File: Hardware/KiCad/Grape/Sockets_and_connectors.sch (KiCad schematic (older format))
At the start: 0 parts

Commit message: Alimentacion terminada
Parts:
- added P1, P10, P11, P12, P13, P14, P15, P16, P17, P18, P19, P2, P20, P21, P22, P3, P4, P5, P6, P7, P8, P9: CONN_01X03, symbol CONN_01X03
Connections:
- new net +5V: P1.2 (P2), P10.2 (P2), P11.2 (P2), P12.2 (P2), P13.2 (P2), P14.2 (P2), P15.2 (P2), P16.2 (P2), P17.2 (P2), P18.2 (P2), P19.2 (P2), P2.2 (P2), P20.2 (P2), P21.2 (P2), P22.2 (P2), P3.2 (P2), P4.2 (P2), P5.2 (P2), P6.2 (P2), P7.2 (P2), P8.2 (P2), P9.2 (P2)
- new net GND: P1.3 (P3), P10.3 (P3), P11.3 (P3), P12.3 (P3), P13.3 (P3), P14.3 (P3), P15.3 (P3), P16.3 (P3), P17.3 (P3), P18.3 (P3), P19.3 (P3), P2.3 (P3), P20.3 (P3), P21.3 (P3), P22.3 (P3), P3.3 (P3), P4.3 (P3), P5.3 (P3), P6.3 (P3), P7.3 (P3), P8.3 (P3), P9.3 (P3)

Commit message: Esquema terminado y  ERC pasado
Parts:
- added P23: I2C, symbol CONN_01X04
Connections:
- net +5V: now also P23.3 (P3)
- net GND: now also P23.4 (P4)
- net RX: now reaches P1.1 (P1)
- net TX: now reaches P6.1 (P1)
- net IO2/PIN2: now reaches P11.1 (P1)
- net IO3/PIN3: now reaches P15.1 (P1)
- net IO4/PIN4: now reaches P19.1 (P1)
- net IO5/PIN5: now reaches P2.1 (P1)
- net IO6/PIN6: now reaches P7.1 (P1)
- net IO7/PIN7: now reaches P12.1 (P1)
- net IO8/PIN8: now reaches P16.1 (P1)
- net IO9/PIN9: now reaches P20.1 (P1)
- net SS/PIN10: now reaches P3.1 (P1)
- net MOSI/PIN11: now reaches P8.1 (P1)
- net MISO/PIN12: now reaches P13.1 (P1)
- net SCK/PIN13: now reaches P17.1 (P1)
- net AD4/SDA: now reaches P21.1 (P1)
- net AD4/SDA: now also P23.1 (P1)
- net AD0: now reaches P4.1 (P1)
- net AD1: now reaches P9.1 (P1)
- net AD2: now reaches P14.1 (P1)
- net AD3: now reaches P18.1 (P1)
- net AD5/SCL: now reaches P22.1 (P1)
- net AD5/SCL: now also P23.2 (P2)
- net AD7: now reaches P5.1 (P1)
- net AD6: now reaches P10.1 (P1)

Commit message: cvpcb terminado
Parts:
- P1, P10, P11, P12, P13, P14, P15, P16, P17, P18, P19, P2, P20, P21, P22, P3, P4, P5, P6, P7, P8, P9: footprint (none) -> Pin_Headers:Pin_Header_Straight_1x03_Pitch1.27mm
- P23: footprint (none) -> Connectors_JST:JST_PH_S4B-PH-K_04x2.00mm_Angled
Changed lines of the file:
@@
 F 0 "P1" H 4100 2300 50  0000 C CNN
 F 1 "CONN_01X03" V 4200 2100 50  0000 C CNN
-F 2 "" H 4100 2100 50  0001 C CNN
+F 2 "Pin_Headers:Pin_Header_Straight_1x03_Pitch1.27mm" H 4100 2100 50  0001 C CNN
 F 3 "" H 4100 2100 50  0001 C CNN
 	1    4100 2100
@@
 F 0 "P6" H 5200 2300 50  0000 C CNN
 F 1 "CONN_01X03" V 5300 2100 50  0000 C CNN
-F 2 "" H 5200 2100 50  0001 C CNN
+F 2 "Pin_Headers:Pin_Header_Straight_1x03_Pitch1.27mm" H 5200 2100 50  0001 C CNN
 F 3 "" H 5200 2100 50  0001 C CNN
 	1    5200 2100
@@
 F 0 "P11" H 6200 2300 50  0000 C CNN
 F 1 "CONN_01X03" V 6300 2100 50  0000 C CNN
-F 2 "" H 6200 2100 50  0001 C CNN
+F 2 "Pin_Headers:Pin_Header_Straight_1x03_Pitch1.27mm" H 6200 2100 50  0001 C CNN
 F 3 "" H 6200 2100 50  0001 C CNN
 	1    6200 2100
@@
 F 0 "P15" H 7200 2300 50  0000 C CNN
 F 1 "CONN_01X03" V 7300 2100 50  0000 C CNN
-F 2 "" H 7200 2100 50  0001 C CNN
+F 2 "Pin_Headers:Pin_Header_Straight_1x03_Pitch1.27mm" H 7200 2100 50  0001 C CNN
 F 3 "" H 7200 2100 50  0001 C CNN
 	1    7200 2100
@@
 F 0 "P19" H 8200 2300 50  0000 C CNN
 F 1 "CONN_01X03" V 8300 2100 50  0000 C CNN
-F 2 "" H 8200 2100 50  0001 C CNN
+F 2 "Pin_Headers:Pin_Header_Straight_1x03_Pitch1.27mm" H 8200 2100 50  0001 C CNN
 F 3 "" H 8200 2100 50  0001 C CNN
 	1    8200 2100
@@
 F 0 "P2" H 4100 3100 50  0000 C CNN
 F 1 "CONN_01X03" V 4200 2900 50  0000 C CNN
-F 2 "" H 4100 2900 50  0001 C CNN
+F 2 "Pin_Headers:Pin_Header_Straight_1x03_Pitch1.27mm" H 4100 2900 50  0001 C CNN
 F 3 "" H 4100 2900 50  0001 C CNN
 	1    4100 2900
@@
 F 0 "P7" H 5200 3100 50  0000 C CNN
 F 1 "CONN_01X03" V 5300 2900 50  0000 C CNN
-F 2 "" H 5200 2900 50  0001 C CNN
+F 2 "Pin_Headers:Pin_Header_Straight_1x03_Pitch1.27mm" H 5200 2900 50  0001 C CNN
 F 3 "" H 5200 2900 50  0001 C CNN
 	1    5200 2900
@@
 F 0 "P12" H 6200 3100 50  0000 C CNN
 F 1 "CONN_01X03" V 6300 2900 50  0000 C CNN
-F 2 "" H 6200 2900 50  0001 C CNN
+F 2 "Pin_Headers:Pin_Header_Straight_1x03_Pitch1.27mm" H 6200 2900 50  0001 C CNN
 F 3 "" H 6200 2900 50  0001 C CNN
 	1    6200 2900
@@
 F 0 "P16" H 7200 3100 50  0000 C CNN
 F 1 "CONN_01X03" V 7300 2900 50  0000 C CNN
-F 2 "" H 7200 2900 50  0001 C CNN
+F 2 "Pin_Headers:Pin_Header_Straight_1x03_Pitch1.27mm" H 7200 2900 50  0001 C CNN
 F 3 "" H 7200 2900 50  0001 C CNN
 	1    7200 2900
@@
 F 0 "P20" H 8200 3100 50  0000 C CNN
 F 1 "CONN_01X03" V 8300 2900 50  0000 C CNN
-F 2 "" H 8200 2900 50  0001 C CNN
+F 2 "Pin_Headers:Pin_Header_Straight_1x03_Pitch1.27mm" H 8200 2900 50  0001 C CNN
 F 3 "" H 8200 2900 50  0001 C CNN
 	1    8200 2900
@@
 F 0 "P3" H 4100 3950 50  0000 C CNN
 F 1 "CONN_01X03" V 4200 3750 50  0000 C CNN
-F 2 "" H 4100 3750 50  0001 C CNN
+F 2 "Pin_Headers:Pin_Header_Straight_1x03_Pitch1.27mm" H 4100 3750 50  0001 C CNN
 F 3 "" H 4100 3750 50  0001 C CNN
 	1    4100 3750
@@
 F 0 "P8" H 5200 3950 50  0000 C CNN
 F 1 "CONN_01X03" V 5300 3750 50  0000 C CNN
-F 2 "" H 5200 3750 50  0001 C CNN
+F 2 "Pin_Headers:Pin_Header_Straight_1x03_Pitch1.27mm" H 5200 3750 50  0001 C CNN
 F 3 "" H 5200 3750 50  0001 C CNN
 	1    5200 3750
@@
 F 0 "P13" H 6200 3950 50  0000 C CNN
 F 1 "CONN_01X03" V 6300 3750 50  0000 C CNN
-F 2 "" H 6200 3750 50  0001 C CNN
+F 2 "Pin_Headers:Pin_Header_Straight_1x03_Pitch1.27mm" H 6200 3750 50  0001 C CNN
 F 3 "" H 6200 3750 50  0001 C CNN
 	1    6200 3750
@@
 F 0 "P17" H 7200 3950 50  0000 C CNN
 F 1 "CONN_01X03" V 7300 3750 50  0000 C CNN
-F 2 "" H 7200 3750 50  0001 C CNN
+F 2 "Pin_Headers:Pin_Header_Straight_1x03_Pitch1.27mm" H 7200 3750 50  0001 C CNN
 F 3 "" H 7200 3750 50  0001 C CNN
 	1    7200 3750
@@
 F 0 "P21" H 8200 3950 50  0000 C CNN
 F 1 "CONN_01X03" V 8300 3750 50  0000 C CNN
-F 2 "" H 8200 3750 50  0001 C CNN
+F 2 "Pin_Headers:Pin_Header_Straight_1x03_Pitch1.27mm" H 8200 3750 50  0001 C CNN
 F 3 "" H 8200 3750 50  0001 C CNN
 	1    8200 3750
@@
 F 0 "P4" H 4100 4750 50  0000 C CNN
 F 1 "CONN_01X03" V 4200 4550 50  0000 C CNN
-F 2 "" H 4100 4550 50  0001 C CNN
+F 2 "Pin_Headers:Pin_Header_Straight_1x03_Pitch1.27mm" H 4100 4550 50  0001 C CNN
 F 3 "" H 4100 4550 50  0001 C CNN
 	1    4100 4550
@@
 F 0 "P9" H 5200 4750 50  0000 C CNN
 F 1 "CONN_01X03" V 5300 4550 50  0000 C CNN
-F 2 "" H 5200 4550 50  0001 C CNN
+F 2 "Pin_Headers:Pin_Header_Straight_1x03_Pitch1.27mm" H 5200 4550 50  0001 C CNN
 F 3 "" H 5200 4550 50  0001 C CNN
 	1    5200 4550
@@
 F 0 "P14" H 6200 4750 50  0000 C CNN
 F 1 "CONN_01X03" V 6300 4550 50  0000 C CNN
-F 2 "" H 6200 4550 50  0001 C CNN
+F 2 "Pin_Headers:Pin_Header_Straight_1x03_Pitch1.27mm" H 6200 4550 50  0001 C CNN
 F 3 "" H 6200 4550 50  0001 C CNN
 	1    6200 4550
@@
 F 0 "P18" H 7200 4750 50  0000 C CNN
 F 1 "CONN_01X03" V 7300 4550 50  0000 C CNN
-F 2 "" H 7200 4550 50  0001 C CNN
+F 2 "Pin_Headers:Pin_Header_Straight_1x03_Pitch1.27mm" H 7200 4550 50  0001 C CNN
 F 3 "" H 7200 4550 50  0001 C CNN
 	1    7200 4550
@@
 F 0 "P22" H 8200 4750 50  0000 C CNN
 F 1 "CONN_01X03" V 8300 4550 50  0000 C CNN
-F 2 "" H 8200 4550 50  0001 C CNN
+F 2 "Pin_Headers:Pin_Header_Straight_1x03_Pitch1.27mm" H 8200 4550 50  0001 C CNN
 F 3 "" H 8200 4550 50  0001 C CNN
 	1    8200 4550
@@
 F 0 "P5" H 4100 5700 50  0000 C CNN
 F 1 "CONN_01X03" V 4200 5500 50  0000 C CNN
-F 2 "" H 4100 5500 50  0001 C CNN
+F 2 "Pin_Headers:Pin_Header_Straight_1x03_Pitch1.27mm" H 4100 5500 50  0001 C CNN
 F 3 "" H 4100 5500 50  0001 C CNN
 	1    4100 5500
@@
 F 0 "P10" H 5200 5700 50  0000 C CNN
 F 1 "CONN_01X03" V 5300 5500 50  0000 C CNN
-F 2 "" H 5200 5500 50  0001 C CNN
+F 2 "Pin_Headers:Pin_Header_Straight_1x03_Pitch1.27mm" H 5200 5500 50  0001 C CNN
 F 3 "" H 5200 5500 50  0001 C CNN
 	1    5200 5500
@@
 F 0 "P23" H 9900 5350 50  0000 C CNN
 F 1 "I2C" V 10000 5100 50  0000 C CNN
-F 2 "" H 9900 5100 50  0001 C CNN
+F 2 "Connectors_JST:JST_PH_S4B-PH-K_04x2.00mm_Angled" H 9900 5100 50  0001 C CNN
 F 3 "" H 9900 5100 50  0001 C CNN
 	1    9900 5100

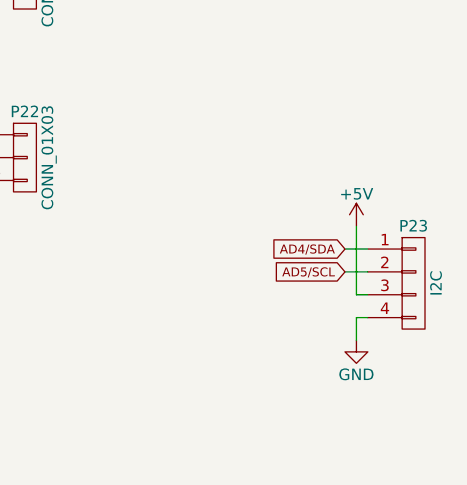
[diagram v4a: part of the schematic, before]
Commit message: Semiconductores colocados en placa y 3D añadido
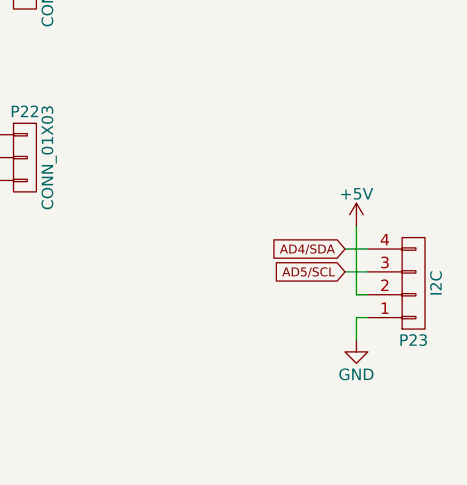
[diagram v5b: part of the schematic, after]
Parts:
- P1, P10, P11, P12, P13, P14, P15, P16, P17, P18, P19, P2, P20, P21, P22, P3, P4, P5, P6, P7, P8, P9: footprint Pin_Headers:Pin_Header_Straight_1x03_Pitch1.27mm -> Pin_Headers:Pin_Header_Straight_1x03_Pitch2.54mm
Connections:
- net +5V: now also P23.2 (P2); no longer P23.3 (P3)
- net AD4/SDA: now also P23.4 (P4); no longer P23.1 (P1)
- net AD5/SCL: now also P23.3 (P3); no longer P23.2 (P2)
- net GND: now also P23.1 (P1); no longer P23.4 (P4)
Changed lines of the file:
@@
 F 0 "P1" H 4100 2300 50  0000 C CNN
 F 1 "CONN_01X03" V 4200 2100 50  0000 C CNN
-F 2 "Pin_Headers:Pin_Header_Straight_1x03_Pitch1.27mm" H 4100 2100 50  0001 C CNN
+F 2 "Pin_Headers:Pin_Header_Straight_1x03_Pitch2.54mm" H 4100 2100 50  0001 C CNN
 F 3 "" H 4100 2100 50  0001 C CNN
 	1    4100 2100
@@
 F 0 "P6" H 5200 2300 50  0000 C CNN
 F 1 "CONN_01X03" V 5300 2100 50  0000 C CNN
-F 2 "Pin_Headers:Pin_Header_Straight_1x03_Pitch1.27mm" H 5200 2100 50  0001 C CNN
+F 2 "Pin_Headers:Pin_Header_Straight_1x03_Pitch2.54mm" H 5200 2100 50  0001 C CNN
 F 3 "" H 5200 2100 50  0001 C CNN
 	1    5200 2100
@@
 F 0 "P11" H 6200 2300 50  0000 C CNN
 F 1 "CONN_01X03" V 6300 2100 50  0000 C CNN
-F 2 "Pin_Headers:Pin_Header_Straight_1x03_Pitch1.27mm" H 6200 2100 50  0001 C CNN
+F 2 "Pin_Headers:Pin_Header_Straight_1x03_Pitch2.54mm" H 6200 2100 50  0001 C CNN
 F 3 "" H 6200 2100 50  0001 C CNN
 	1    6200 2100
@@
 F 0 "P15" H 7200 2300 50  0000 C CNN
 F 1 "CONN_01X03" V 7300 2100 50  0000 C CNN
-F 2 "Pin_Headers:Pin_Header_Straight_1x03_Pitch1.27mm" H 7200 2100 50  0001 C CNN
+F 2 "Pin_Headers:Pin_Header_Straight_1x03_Pitch2.54mm" H 7200 2100 50  0001 C CNN
 F 3 "" H 7200 2100 50  0001 C CNN
 	1    7200 2100
@@
 F 0 "P19" H 8200 2300 50  0000 C CNN
 F 1 "CONN_01X03" V 8300 2100 50  0000 C CNN
-F 2 "Pin_Headers:Pin_Header_Straight_1x03_Pitch1.27mm" H 8200 2100 50  0001 C CNN
+F 2 "Pin_Headers:Pin_Header_Straight_1x03_Pitch2.54mm" H 8200 2100 50  0001 C CNN
 F 3 "" H 8200 2100 50  0001 C CNN
 	1    8200 2100
@@
 F 0 "P2" H 4100 3100 50  0000 C CNN
 F 1 "CONN_01X03" V 4200 2900 50  0000 C CNN
-F 2 "Pin_Headers:Pin_Header_Straight_1x03_Pitch1.27mm" H 4100 2900 50  0001 C CNN
+F 2 "Pin_Headers:Pin_Header_Straight_1x03_Pitch2.54mm" H 4100 2900 50  0001 C CNN
 F 3 "" H 4100 2900 50  0001 C CNN
 	1    4100 2900
@@
 F 0 "P7" H 5200 3100 50  0000 C CNN
 F 1 "CONN_01X03" V 5300 2900 50  0000 C CNN
-F 2 "Pin_Headers:Pin_Header_Straight_1x03_Pitch1.27mm" H 5200 2900 50  0001 C CNN
+F 2 "Pin_Headers:Pin_Header_Straight_1x03_Pitch2.54mm" H 5200 2900 50  0001 C CNN
 F 3 "" H 5200 2900 50  0001 C CNN
 	1    5200 2900
@@
 F 0 "P12" H 6200 3100 50  0000 C CNN
 F 1 "CONN_01X03" V 6300 2900 50  0000 C CNN
-F 2 "Pin_Headers:Pin_Header_Straight_1x03_Pitch1.27mm" H 6200 2900 50  0001 C CNN
+F 2 "Pin_Headers:Pin_Header_Straight_1x03_Pitch2.54mm" H 6200 2900 50  0001 C CNN
 F 3 "" H 6200 2900 50  0001 C CNN
 	1    6200 2900
@@
 F 0 "P16" H 7200 3100 50  0000 C CNN
 F 1 "CONN_01X03" V 7300 2900 50  0000 C CNN
-F 2 "Pin_Headers:Pin_Header_Straight_1x03_Pitch1.27mm" H 7200 2900 50  0001 C CNN
+F 2 "Pin_Headers:Pin_Header_Straight_1x03_Pitch2.54mm" H 7200 2900 50  0001 C CNN
 F 3 "" H 7200 2900 50  0001 C CNN
 	1    7200 2900
@@
 F 0 "P20" H 8200 3100 50  0000 C CNN
 F 1 "CONN_01X03" V 8300 2900 50  0000 C CNN
-F 2 "Pin_Headers:Pin_Header_Straight_1x03_Pitch1.27mm" H 8200 2900 50  0001 C CNN
+F 2 "Pin_Headers:Pin_Header_Straight_1x03_Pitch2.54mm" H 8200 2900 50  0001 C CNN
 F 3 "" H 8200 2900 50  0001 C CNN
 	1    8200 2900
@@
 F 0 "P3" H 4100 3950 50  0000 C CNN
 F 1 "CONN_01X03" V 4200 3750 50  0000 C CNN
-F 2 "Pin_Headers:Pin_Header_Straight_1x03_Pitch1.27mm" H 4100 3750 50  0001 C CNN
+F 2 "Pin_Headers:Pin_Header_Straight_1x03_Pitch2.54mm" H 4100 3750 50  0001 C CNN
 F 3 "" H 4100 3750 50  0001 C CNN
 	1    4100 3750
@@
 F 0 "P8" H 5200 3950 50  0000 C CNN
 F 1 "CONN_01X03" V 5300 3750 50  0000 C CNN
-F 2 "Pin_Headers:Pin_Header_Straight_1x03_Pitch1.27mm" H 5200 3750 50  0001 C CNN
+F 2 "Pin_Headers:Pin_Header_Straight_1x03_Pitch2.54mm" H 5200 3750 50  0001 C CNN
 F 3 "" H 5200 3750 50  0001 C CNN
 	1    5200 3750
@@
 F 0 "P13" H 6200 3950 50  0000 C CNN
 F 1 "CONN_01X03" V 6300 3750 50  0000 C CNN
-F 2 "Pin_Headers:Pin_Header_Straight_1x03_Pitch1.27mm" H 6200 3750 50  0001 C CNN
+F 2 "Pin_Headers:Pin_Header_Straight_1x03_Pitch2.54mm" H 6200 3750 50  0001 C CNN
 F 3 "" H 6200 3750 50  0001 C CNN
 	1    6200 3750
@@
 F 0 "P17" H 7200 3950 50  0000 C CNN
 F 1 "CONN_01X03" V 7300 3750 50  0000 C CNN
-F 2 "Pin_Headers:Pin_Header_Straight_1x03_Pitch1.27mm" H 7200 3750 50  0001 C CNN
+F 2 "Pin_Headers:Pin_Header_Straight_1x03_Pitch2.54mm" H 7200 3750 50  0001 C CNN
 F 3 "" H 7200 3750 50  0001 C CNN
 	1    7200 3750
@@
 F 0 "P21" H 8200 3950 50  0000 C CNN
 F 1 "CONN_01X03" V 8300 3750 50  0000 C CNN
-F 2 "Pin_Headers:Pin_Header_Straight_1x03_Pitch1.27mm" H 8200 3750 50  0001 C CNN
+F 2 "Pin_Headers:Pin_Header_Straight_1x03_Pitch2.54mm" H 8200 3750 50  0001 C CNN
 F 3 "" H 8200 3750 50  0001 C CNN
 	1    8200 3750
@@
 F 0 "P4" H 4100 4750 50  0000 C CNN
 F 1 "CONN_01X03" V 4200 4550 50  0000 C CNN
-F 2 "Pin_Headers:Pin_Header_Straight_1x03_Pitch1.27mm" H 4100 4550 50  0001 C CNN
+F 2 "Pin_Headers:Pin_Header_Straight_1x03_Pitch2.54mm" H 4100 4550 50  0001 C CNN
 F 3 "" H 4100 4550 50  0001 C CNN
 	1    4100 4550
@@
 F 0 "P9" H 5200 4750 50  0000 C CNN
 F 1 "CONN_01X03" V 5300 4550 50  0000 C CNN
-F 2 "Pin_Headers:Pin_Header_Straight_1x03_Pitch1.27mm" H 5200 4550 50  0001 C CNN
+F 2 "Pin_Headers:Pin_Header_Straight_1x03_Pitch2.54mm" H 5200 4550 50  0001 C CNN
 F 3 "" H 5200 4550 50  0001 C CNN
 	1    5200 4550
@@
 F 0 "P14" H 6200 4750 50  0000 C CNN
 F 1 "CONN_01X03" V 6300 4550 50  0000 C CNN
-F 2 "Pin_Headers:Pin_Header_Straight_1x03_Pitch1.27mm" H 6200 4550 50  0001 C CNN
+F 2 "Pin_Headers:Pin_Header_Straight_1x03_Pitch2.54mm" H 6200 4550 50  0001 C CNN
 F 3 "" H 6200 4550 50  0001 C CNN
 	1    6200 4550
@@
 F 0 "P18" H 7200 4750 50  0000 C CNN
 F 1 "CONN_01X03" V 7300 4550 50  0000 C CNN
-F 2 "Pin_Headers:Pin_Header_Straight_1x03_Pitch1.27mm" H 7200 4550 50  0001 C CNN
+F 2 "Pin_Headers:Pin_Header_Straight_1x03_Pitch2.54mm" H 7200 4550 50  0001 C CNN
 F 3 "" H 7200 4550 50  0001 C CNN
 	1    7200 4550
@@
 F 0 "P22" H 8200 4750 50  0000 C CNN
 F 1 "CONN_01X03" V 8300 4550 50  0000 C CNN
-F 2 "Pin_Headers:Pin_Header_Straight_1x03_Pitch1.27mm" H 8200 4550 50  0001 C CNN
+F 2 "Pin_Headers:Pin_Header_Straight_1x03_Pitch2.54mm" H 8200 4550 50  0001 C CNN
 F 3 "" H 8200 4550 50  0001 C CNN
 	1    8200 4550
@@
 F 0 "P5" H 4100 5700 50  0000 C CNN
 F 1 "CONN_01X03" V 4200 5500 50  0000 C CNN
-F 2 "Pin_Headers:Pin_Header_Straight_1x03_Pitch1.27mm" H 4100 5500 50  0001 C CNN
+F 2 "Pin_Headers:Pin_Header_Straight_1x03_Pitch2.54mm" H 4100 5500 50  0001 C CNN
 F 3 "" H 4100 5500 50  0001 C CNN
 	1    4100 5500
@@
 F 0 "P10" H 5200 5700 50  0000 C CNN
 F 1 "CONN_01X03" V 5300 5500 50  0000 C CNN
-F 2 "Pin_Headers:Pin_Header_Straight_1x03_Pitch1.27mm" H 5200 5500 50  0001 C CNN
+F 2 "Pin_Headers:Pin_Header_Straight_1x03_Pitch2.54mm" H 5200 5500 50  0001 C CNN
 F 3 "" H 5200 5500 50  0001 C CNN
 	1    5200 5500
@@
 F 3 "" H 9900 5100 50  0001 C CNN
 	1    9900 5100
-	1    0    0    -1
-$EndComp
-Wire Wire Line
+	1    0    0    1
+$EndComp
+Wire Wire Line
